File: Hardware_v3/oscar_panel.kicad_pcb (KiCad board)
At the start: 2 copper layers, 71 x 128.5 mm, 15 parts

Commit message: Started working on panel
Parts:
- removed the G*** at (150.3, 113.7)
- added G***: LOGO, oscar_logo:oscar_logo2, F.Cu at (136.7, 41.6)
- added REF**: USB_C_Cutout, Custom_Footprints:USB_C_Cutout, F.Cu at (150.4, 144.1)
- added Ref**: Thonkikonn_6.1mm, Custom_Footprints:MountingHole_6.3mm, F.Cu at (109.4, 120.0)
- added Ref**: Thonkikonn_6.1mm, Custom_Footprints:MountingHole_6.3mm, F.Cu at (124.4, 120.0)
- added Ref**: Thonkikonn_6.1mm, Custom_Footprints:MountingHole_6.3mm, F.Cu at (139.2, 120.0)
- added Ref**: Thonkiconn_Socket_MountingHole_6mm, Custom_Footprints:Thonkiconn_Socket_MountingHole_6mm, F.Cu at (161.8, 145.2)
- moved Ref** 40.6 mm to (150.4, 131.5)
- moved Ref** 26.4 mm to (159.2, 105.0)
- moved Ref** 26.4 mm to (111.2, 105.0)
- moved Ref** 26.2 mm to (109.4, 145.2)
- moved Ref** 26.2 mm to (124.4, 145.2)
- moved Ref** 26.2 mm to (139.4, 145.2)
- moved Ref** 26.1 mm to (109.4, 132.0)
- moved Ref** 26.1 mm to (124.4, 132.0)
- moved Ref** 26.1 mm to (139.4, 132.0)
- moved Ref** 25.7 mm to (107.5, 37.9)
- moved Ref** 25.7 mm to (163.5, 37.9)
- moved Ref** 25.7 mm to (107.5, 160.4)
- moved Ref** 25.7 mm to (163.5, 160.4)
- moved Ref** 24.9 mm to (161.8, 131.2)
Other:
- outline, holes or cut-outs redrawn
- net class Default removed
- board text added: "OSCAR Panel v3"
- board text removed: "OSCAR Panel v2"

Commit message: Control Layout change
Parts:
- removed the Ref** at (150.4, 131.5)
- removed the Ref** at (109.4, 120.0)
- removed the Ref** at (139.2, 120.0)
- added Ref**: Thonkikonn_6.1mm, Custom_Footprints:MountingHole_6.3mm, F.Cu at (152.0, 120.0)
- added Ref**: Thonkikonn_6.1mm, Custom_Footprints:MountingHole_6.3mm, F.Cu at (122.0, 120.0)
- added Ref**: Push_Button_Hole, Custom_Footprints:Small_Pushbutton_Hole_3.5mm, F.Cu at (164.0, 131.5)
- added Ref**: Push_Button_Hole, Custom_Footprints:Tall_Trimmer_Hole, F.Cu at (135.5, 103.0)
- added kibuzzard-67F2B0DF: G***, kibuzzard-67F2B0DF, F.Cu at (135.5, 94.0)
- added kibuzzard-67F2B10D: G***, kibuzzard-67F2B10D, F.Cu at (107.6, 124.5)
- added kibuzzard-67F2B157: G***, kibuzzard-67F2B157, F.Cu at (164.0, 124.7)
- moved Ref** 54.2 mm to (107.6, 132.0)
- moved Ref** 54.2 mm to (107.6, 145.2)
- moved REF** 13.6 mm to (164.0, 144.1)
- moved Ref** 12.6 mm to (122.0, 132.0)
- moved Ref** 12.6 mm to (137.0, 120.0)
- moved Ref** 12.6 mm to (137.0, 132.0)
- moved Ref** 12.6 mm to (152.0, 132.0)
- moved Ref** 12.6 mm to (122.0, 145.2)
- moved Ref** 12.6 mm to (137.0, 145.2)
- moved Ref** 12.6 mm to (152.0, 145.2)
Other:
- board text removed: "MIDI"
- board text removed: "Menu"
- board text removed: "Mode"
- board text removed: "Reset"

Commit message: More layout
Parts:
- removed the Ref** at (135.5, 103.0)
- removed kibuzzard-67F2B0DF: G***, kibuzzard-67F2B0DF
- added Ref**: Push_Button_Hole, Custom_Footprints:Small_Pushbutton_Hole_3.5mm, F.Cu at (135.5, 101.0)
- added kibuzzard-67F7FC1B: G***, kibuzzard-67F7FC1B, F.Cu at (122.0, 113.3)
- added kibuzzard-67F7FC29: G***, kibuzzard-67F7FC29, F.Cu at (152.0, 113.3)
- added kibuzzard-67F7FC30: G***, kibuzzard-67F7FC30, F.Cu at (137.0, 113.3)
- added kibuzzard-67F8D614: G***, kibuzzard-67F8D614, F.Cu at (135.5, 94.2)
- moved kibuzzard-67F2B10D 0.20 mm to (107.6, 124.7)
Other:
- outline, holes or cut-outs redrawn
- board text removed: "In"
- board text removed: "Out"

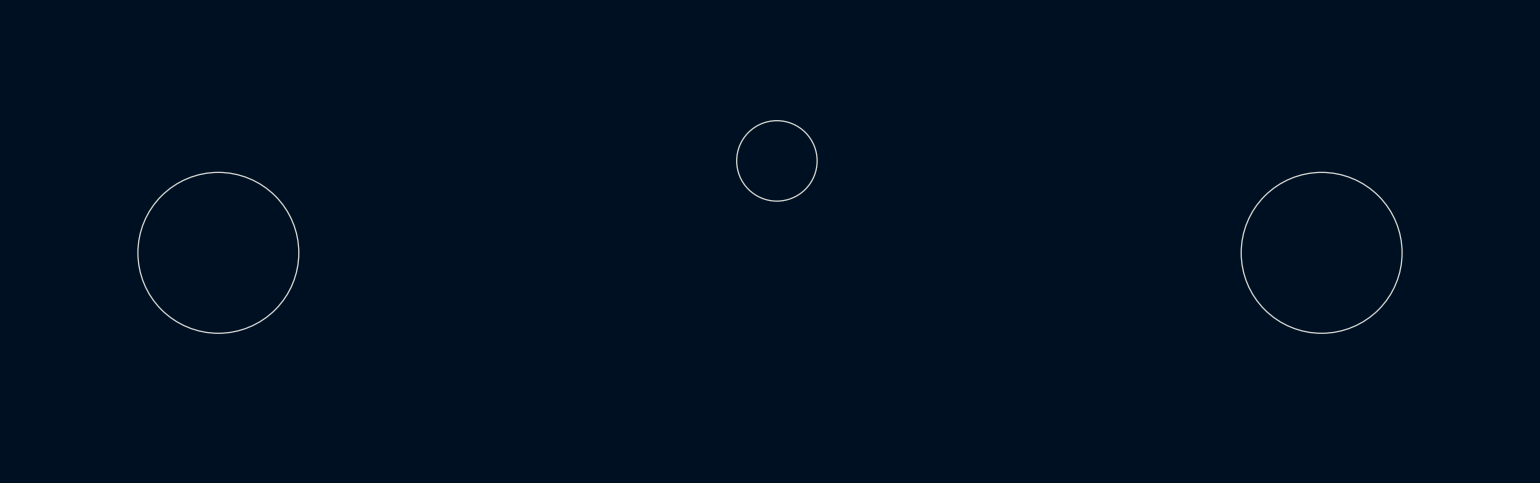
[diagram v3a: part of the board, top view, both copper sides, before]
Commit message: Started updating firmware to v2a
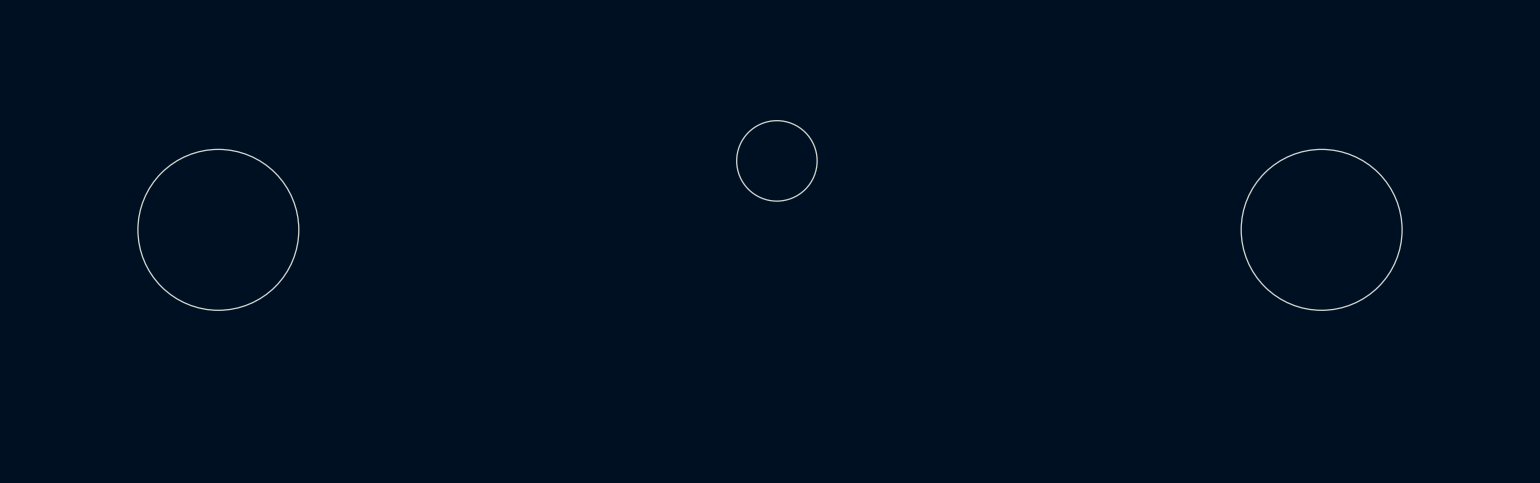
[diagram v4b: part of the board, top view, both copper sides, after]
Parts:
- moved Ref** 1.00 mm to (159.2, 104.0)
- moved Ref** 1.00 mm to (111.2, 104.0)
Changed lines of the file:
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@@
 	(footprint "Custom_Footprints:Alpha_9mm_pot_hole"
 		(layer "F.Cu")
-		(at 159.2 105)
+		(at 159.2 104)
 		(descr "Mounting Hole 7mm")
 		(tags "mounting hole 7mm")
@@
 	(footprint "Custom_Footprints:Alpha_9mm_pot_hole"
 		(layer "F.Cu")
-		(at 111.2 105)
+		(at 111.2 104)
 		(descr "Mounting Hole 7mm")
 		(tags "mounting hole 7mm")
@@
 	)
 	(gr_circle
-		(center 111.2 105)
-		(end 119.3 105.8)
+		(center 111.2 104)
+		(end 119.3 104.8)
 		(stroke
 			(width 0.05)
@@
 	(gr_poly
 		(pts
-			(xy 112 96) (xy 109 93) (xy 112 90)
+			(xy 112 95) (xy 109 92) (xy 112 89)
 		)
 		(stroke
@@
 	)
 	(gr_circle
-		(center 159.2 105)
-		(end 167.3 105.8)
+		(center 159.2 104)
+		(end 167.3 104.8)
 		(stroke
 			(width 0.05)

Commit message: V3 production files submitted to JLC
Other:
- board text removed: "A"
- board text removed: "B"
- board text removed: "C"
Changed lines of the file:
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@@
 		(allow_soldermask_bridges_in_footprints no)
 		(pcbplotparams
-			(layerselection 0x00010fc_ffffffff)
+			(layerselection 0x00010f0_ffffffff)
 			(plot_on_all_layers_selection 0x0000000_00000000)
 			(disableapertmacros no)
@@
 			(drillshape 0)
 			(scaleselection 1)
-			(outputdirectory "Panel_Gerbers/")
+			(outputdirectory "Gerbers/Panel/")
 		)
 	)
@@
 				(font
 					(size 0.001 0.001)
+					(thickness 0.15)
 				)
 			)
@@
 				(font
 					(size 0.001 0.001)
+					(thickness 0.15)
 				)
 			)
@@
 		)
 	)
-	(gr_text "A"
-		(at 36.8 108.5 0)
-		(layer "F.Mask")
-		(effects
-			(font
-				(size 2 2)
-				(thickness 0.3)
-			)
-		)
-	)
-	(gr_text "B"
-		(at 51.8 108.5 0)
-		(layer "F.Mask")
-		(effects
-			(font
-				(size 2 2)
-				(thickness 0.3)
-			)
-		)
-	)
-	(gr_text "C"
-		(at 66.8 108.5 0)
-		(layer "F.Mask")
-		(effects
-			(font
-				(size 2 2)
-				(thickness 0.3)
-			)
-		)
-	)
 	(gr_text "Mountjoy Modular"
 		(at 125.6 160.3 0)
@@
 		)
 	)
-	(gr_text "A"
-		(at 31.9 118.2 0)
-		(layer "F.Mask")
-		(effects
-			(font
-				(size 2 2)
-				(thickness 0.3)
-			)
-		)
-	)
-	(gr_text "B"
-		(at 46.9 118.2 0)
-		(layer "F.Mask")
-		(effects
-			(font
-				(size 2 2)
-				(thickness 0.3)
-			)
-		)
-	)
-	(gr_text "C"
-		(at 61.9 118.2 0)
-		(layer "F.Mask")
-		(effects
-			(font
-				(size 2 2)
-				(thickness 0.3)
-			)
-		)
-	)

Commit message: USB bootloader working
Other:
- board text added: "OSCAR Panel v3.1"
- board text removed: "OSCAR Panel v3"
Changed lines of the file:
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@@
 	(gr_poly
 		(pts
-			(xy 160 90) (xy 163 93) (xy 160 96)
+			(xy 160 89) (xy 163 92) (xy 160 95)
 		)
 		(stroke
@@
 		(layer "Edge.Cuts")
 	)
-	(gr_text "OSCAR Panel v3"
+	(gr_text "OSCAR Panel v3.1"
 		(at 135 38.3 0)
 		(layer "B.SilkS")
